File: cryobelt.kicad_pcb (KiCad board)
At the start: 4 copper layers, 90 x 50 mm, 96 parts, among them J1 Speaker, J2 Charge, J3 Battery, J4 Battery, Q1 AO3401A, Q2 AO3400A, Q3 AO3401A, Q4 AO3400A, SW1 Reset, SW2 Boot, SW3 Down, SW4 User, SW5 Up, U1 SHT4x, U2 ESP32-S3-MINI-1, U3 MAX98357A, U4 FUSB303BTMX, U5 TPS61089, U6 D3V3XA4B10LP, U7 BQ25895RTW, U8 TPS63001, U9 INA180A3

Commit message: Reset PCB
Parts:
- removed R29: 1k, Resistor_SMD:R_0603_1608Metric
- removed R30: 100R, Resistor_SMD:R_0603_1608Metric
- removed R31: 100k, Resistor_SMD:R_0603_1608Metric
- added C31: 1uF, Capacitor_SMD:C_0603_1608Metric, F.Cu at (232.7, 113.1)
- added C32: 10uF, Capacitor_SMD:C_0603_1608Metric, F.Cu at (232.7, 115.6)
- C1, C10, C11, C12, C15, C23, C25, C30, C8, C9, L3, Q2, Q3, R1, R12, R13, R14, R16, R17, R18, R2, R3, R4, R5, R6, R7, R9, TH1, U3, U5, U6, U7, U8: moved to F.Cu
- R20: value 10k -> 100R
- R21: value 10k -> 2.2k
- R22: value 10k -> 30.1k; moved to F.Cu
- R23: value 100R -> 5.23k; moved to F.Cu
- R24: value 2.2k -> 10k
- R25: value 30.1k -> 0.05R/0.1%; footprint Resistor_SMD:R_0603_1608Metric -> Resistor_SMD:R_1206_3216Metric
- R26: value 5.23k -> 1k
- R27: value 10k -> 100R; moved to F.Cu
- R28: value 0.05R/0.1% -> 100k; footprint Resistor_SMD:R_1206_3216Metric -> Resistor_SMD:R_0603_1608Metric; moved to F.Cu
- moved C2 125.9 mm to (243.2, 87.3), turned to 0 degrees
- moved C5 122.7 mm to (243.2, 94.8), turned to 0 degrees
- moved C4 122.1 mm to (243.2, 92.3), turned to 0 degrees
- moved J4 103.0 mm to (237.0, 108.9), turned to 0 degrees
- moved Q4 102.3 mm to (237.1, 121.2), turned to 0 degrees
- moved Q1 102.1 mm to (225.6, 85.7), turned to 0 degrees
- moved Q3 99.0 mm to (225.6, 94.6), turned to 0 degrees
- moved R4 98.3 mm to (251.2, 84.8), turned to 0 degrees
- moved R3 97.2 mm to (247.2, 97.3)
- moved C7 97.1 mm to (247.2, 84.8)
- moved C30 95.2 mm to (232.7, 110.6), turned to 0 degrees
- moved J1 94.1 mm to (233.0, 102.7), turned to 0 degrees
- moved C6 94.1 mm to (243.2, 97.3)
- moved R7 92.7 mm to (251.2, 92.3)
- moved U9 92.4 mm to (237.3, 116.7), turned to 0 degrees
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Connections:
- R20 pad 1: /ESP32-S3/SCL -> VDC
- R20 pad 2: +3V3 -> Net-(U8-EN)
- R21 pad 1: /ESP32-S3/SDA -> Net-(U7-STAT)
- R21 pad 2: +3V3 -> Net-(D4-K)
- R22 pad 1: /ESP32-S3/~{BQ_INT} -> Net-(U7-TS)
- R22 pad 2: +3V3 -> GND
- R23 pad 1: VDC -> Net-(U7-REGN)
- R23 pad 2: Net-(U8-EN) -> Net-(U7-TS)
- R24 pad 1: Net-(U7-STAT) -> Net-(U7-DSEL)
- R24 pad 2: Net-(D4-K) -> +3V3
- R25 pad 1: Net-(U7-TS) -> +12V
- R25 pad 2: GND -> /Fan Control/FAN+
- R26 pad 1: Net-(U7-REGN) -> /ESP32-S3/I_FAN
- R26 pad 2: Net-(U7-TS) -> Net-(R26-Pad2)
- R27 pad 1: Net-(U7-DSEL) -> /ESP32-S3/FAN_GATE
- R27 pad 2: +3V3 -> Net-(Q4-G)
- R28 pad 1: +12V -> GND
- R28 pad 2: /Fan Control/FAN+ -> Net-(Q4-G)
- U9 pad 1: Net-(R29-Pad2) -> Net-(R26-Pad2)
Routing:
- net GND: track 120.4 -> 0.00 mm, vias 64 -> 0
- net /ESP32-S3/SDA: track 118.9 -> 0.00 mm, vias 2 -> 0
- net /ESP32-S3/SCL: track 118.3 -> 0.00 mm, vias 4 -> 0
- net VBUS: track 105.8 -> 0.00 mm, vias 4 -> 0
- net VDC: track 93.0 -> 0.00 mm, vias 6 -> 0
- net Net-(U2-IO38): track 90.7 -> 0.00 mm
- net /ESP32-S3/DOUT: track 80.9 -> 0.00 mm, vias 1 -> 0
- net /Power/PMID: track 75.5 -> 0.00 mm, vias 3 -> 0
- net /ESP32-S3/~{BQ_INT}: track 68.2 -> 0.00 mm, vias 3 -> 0
- net Net-(U2-IO40): track 66.6 -> 0.00 mm
- net /Power/SW: track 66.4 -> 0.00 mm, vias 7 -> 0
- net /ESP32-S3/12V_EN: track 59.8 -> 0.00 mm, vias 3 -> 0
- net /ESP32-S3/I_FAN: track 59.4 -> 0.00 mm, vias 3 -> 0
- net Net-(U2-IO39): track 58.5 -> 0.00 mm
- net Net-(R29-Pad2): track 49.7 -> 0.00 mm, vias 2 -> 0
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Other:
- outline, holes or cut-outs redrawn

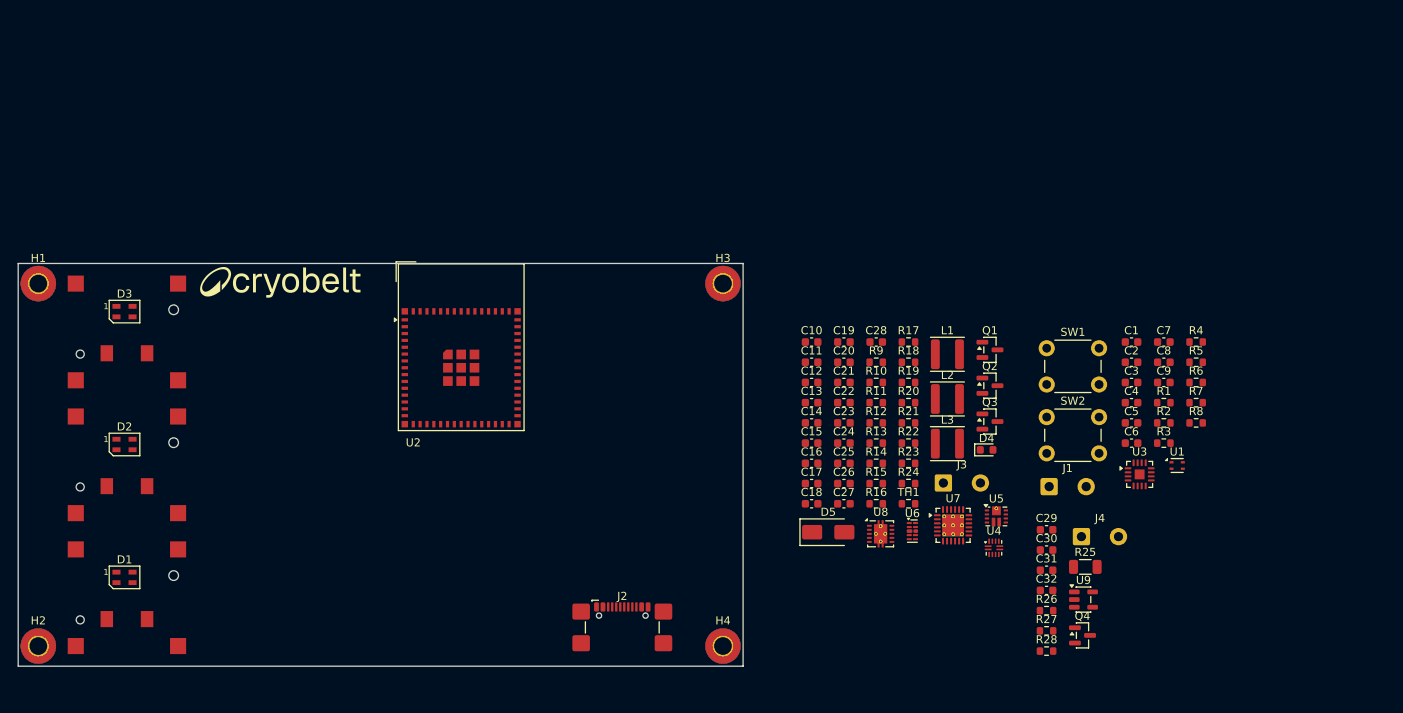
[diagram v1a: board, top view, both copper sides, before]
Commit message: Group power components
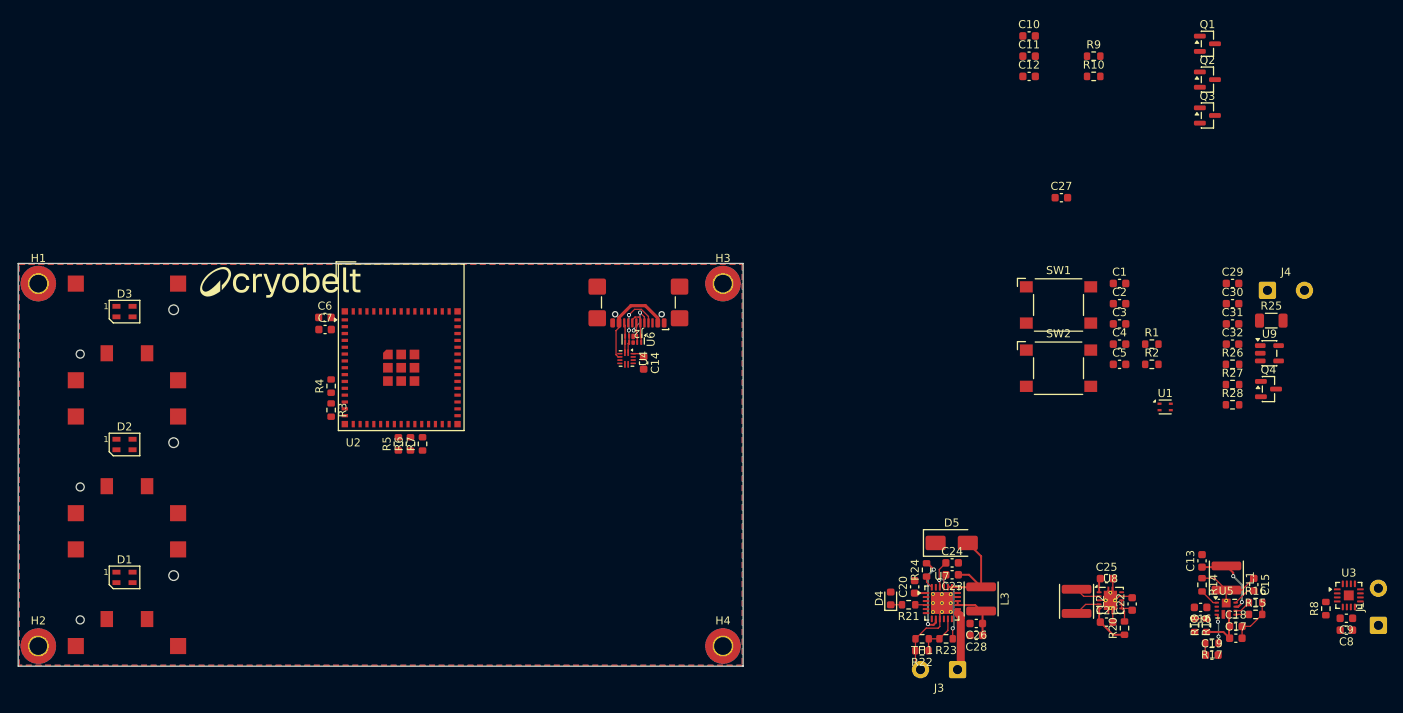
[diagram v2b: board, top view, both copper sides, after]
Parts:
- removed R11, R12, R13: 10k, Resistor_SMD:R_0603_1608Metric
- SW1, SW2: footprint Button_Switch_THT:SW_PUSH_6mm -> Button_Switch_SMD:SW_SPST_Omron_B3FS-100xP
- moved R4 107.5 mm to (143.8, 90.2), turned to 90 degrees
- moved C7 104.1 mm to (143.1, 83.2)
- moved R3 103.5 mm to (143.8, 93.2), turned to -90 degrees
- moved C6 101.4 mm to (143.1, 81.7)
- moved R5 99.6 mm to (152.2, 97.4), turned to 90 degrees
- moved R6 97.8 mm to (153.7, 97.4), turned to 90 degrees
- moved R7 96.2 mm to (155.2, 97.4), turned to 90 degrees
- moved C19 60.0 mm to (253.2, 123.6)
- moved C15 57.6 mm to (258.4, 114.9), turned to -90 degrees
- moved C17 56.1 mm to (256.2, 121.5)
- moved C18 54.8 mm to (256.2, 120.0)
- moved R17 53.1 mm to (253.2, 122.2), turned to 180 degrees
- moved C13 52.3 mm to (252.0, 111.9), turned to 90 degrees
- moved C16 51.5 mm to (251.8, 117.7), turned to 180 degrees
- moved U4 51.3 mm to (180.5, 86.8), turned to -90 degrees
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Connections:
- R7 pad 2: Net-(U2-IO21) -> Net-(U2-IO26)
- U2 pad 25: Net-(U2-IO21) -> unconnected-(U2-IO21-Pad25)
- U2 pad 26: unconnected-(U2-IO26-Pad26) -> Net-(U2-IO26)
- U2 pad 32: unconnected-(U2-IO36-Pad32) -> /ESP32-S3/OUT1
- U2 pad 33: unconnected-(U2-IO37-Pad33) -> /ESP32-S3/OUT2
- U2 pad 41: /ESP32-S3/OUT1 -> unconnected-(U2-IO45-Pad41)
- U2 pad 44: /ESP32-S3/OUT2 -> unconnected-(U2-IO46-Pad44)
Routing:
- net GND: track 0.00 -> 22.7 mm
- net VDC: track 0.00 -> 21.7 mm, vias 0 -> 2
- net /Power/SW: track 0.00 -> 13.7 mm
- net VBUS: track 0.00 -> 13.4 mm
- net +3V3: track 0.00 -> 13.1 mm, vias 0 -> 2
- net Net-(U7-REGN): track 0.00 -> 11.9 mm, vias 0 -> 2
- net Net-(U5-SW): track 0.00 -> 9.26 mm
- net /Power/CC1: track 0.00 -> 8.62 mm, vias 0 -> 2
- net +BATT: track 0.00 -> 7.84 mm
- net /ESP32-S3/D-: track 0.00 -> 6.85 mm, vias 0 -> 2
- net +12V: track 0.00 -> 6.19 mm
- net Net-(U7-TS): track 0.00 -> 5.72 mm
- net /ESP32-S3/D+: track 0.00 -> 4.63 mm
- net Net-(U8-EN): track 0.00 -> 4.16 mm
- net /Power/CC2: track 0.00 -> 3.75 mm
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- added copper zone on B.Cu, net GND
- added copper zone on F.Cu, net GND

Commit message: Fully routed, no DRC errors
tysm Kevin :D
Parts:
- C2, C4, C5: footprint Capacitor_SMD:C_0603_1608Metric -> Capacitor_SMD:C_0402_1005Metric
- J4: value Battery -> Fan
- moved J1 146.1 mm to (131.5, 87.5), turned to 0 degrees
- moved C8 143.9 mm to (130.9, 83.5), turned to 90 degrees
- moved C9 142.1 mm to (132.3, 83.5), turned to 90 degrees
- moved U1 140.1 mm to (107.5, 100.1), turned to 90 degrees
- moved U3 138.9 mm to (135.2, 83.8), turned to -90 degrees
- moved R8 138.8 mm to (133.5, 80.9), turned to 0 degrees
- moved C3 133.7 mm to (109.2, 100.2), turned to 90 degrees
- moved J4 130.6 mm to (131.8, 102.7)
- moved R25 127.5 mm to (133.5, 93.2), turned to 180 degrees
- moved C29 127.3 mm to (130.1, 97.6), turned to 180 degrees
- moved C32 127.2 mm to (129.0, 95.2), turned to -90 degrees
- moved U9 127.1 mm to (133.6, 96.1), turned to 180 degrees
- moved C31 125.9 mm to (130.5, 95.2), turned to -90 degrees
- moved C2 125.4 mm to (121.1, 114.2), turned to -90 degrees
- moved C30 123.3 mm to (134.1, 100.0), turned to 180 degrees
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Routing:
- net GND: track 22.7 -> 148.0 mm, vias 0 -> 69
- net VDC: track 21.7 -> 134.2 mm, vias 2 -> 3
- net /ESP32-S3/SCL: track 0.00 -> 89.3 mm, vias 0 -> 4
- net /ESP32-S3/SDA: track 0.00 -> 89.3 mm, vias 0 -> 4
- net Net-(U2-IO40): track 0.00 -> 79.4 mm
- net Net-(U2-IO39): track 0.00 -> 61.5 mm
- net /ESP32-S3/OTG_GATE: track 0.00 -> 61.2 mm, vias 0 -> 2
- net /ESP32-S3/DIN: track 0.00 -> 52.8 mm
- net /ESP32-S3/OUT1: track 0.00 -> 49.2 mm
- net /ESP32-S3/~{BQ_INT}: track 0.00 -> 47.2 mm, vias 0 -> 2
- net Net-(U2-IO38): track 0.00 -> 46.7 mm, vias 0 -> 2
- net /ESP32-S3/DOUT: track 0.00 -> 46.2 mm, vias 0 -> 2
- net /ESP32-S3/D-: track 6.85 -> 45.5 mm, vias 2 -> 3
- net /ESP32-S3/D+: track 4.63 -> 41.2 mm, vias 0 -> 2
- net +12V: track 6.19 -> 40.7 mm
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- removed copper zone on B.Cu, net GND
- removed copper zone on F.Cu, net GND
